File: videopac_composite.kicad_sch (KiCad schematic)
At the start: 17 parts, among them J102 Composite Output, J104 Composite Input, Q101 BC548, Q102 BC558, Q103 BC548

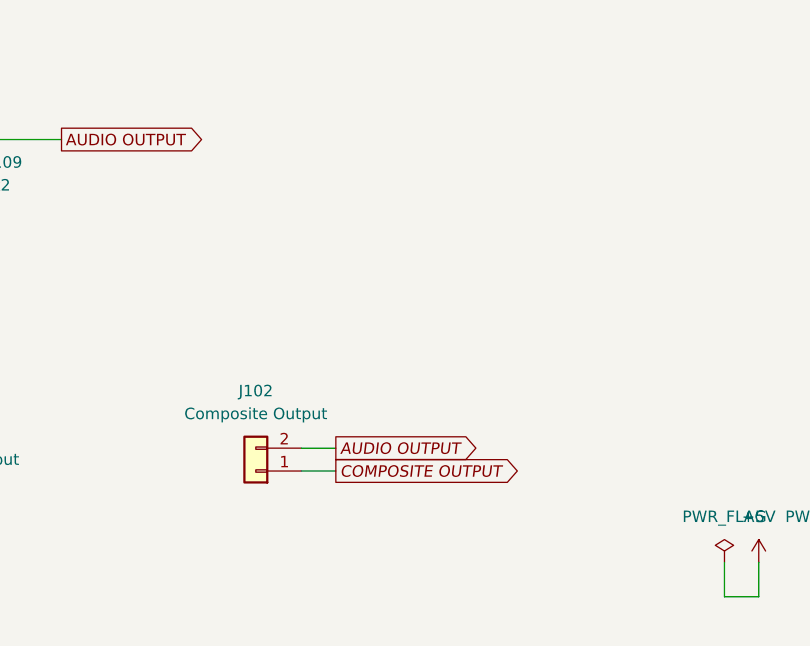
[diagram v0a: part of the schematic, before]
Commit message: Add additional ground connections.
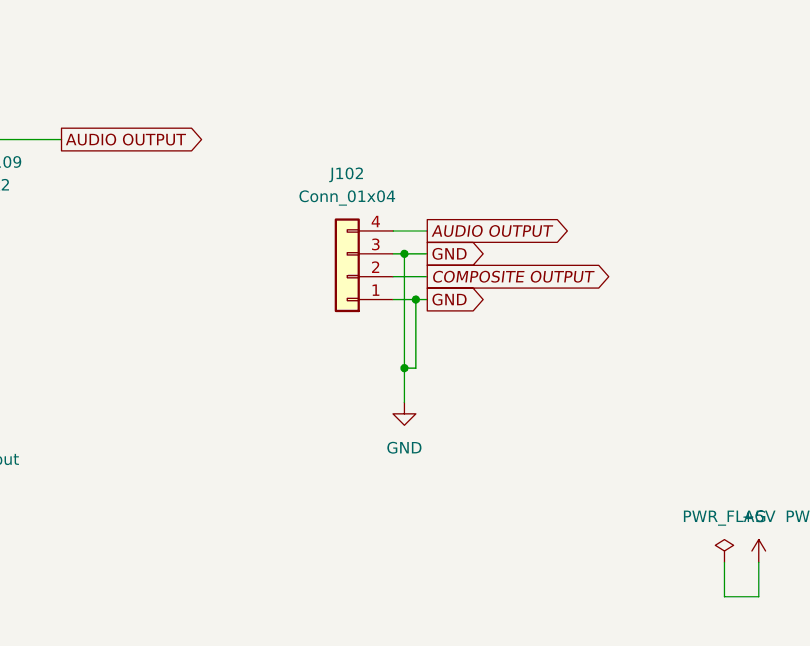
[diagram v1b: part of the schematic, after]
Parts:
- removed J102: Composite Output, Connector_PinHeader_2.54mm:PinHeader_1x02_P2.54mm_Horizontal, symbol Connector_Generic:Conn_01x02
- added J102: Conn_01x04, Connector_PinHeader_2.54mm:PinHeader_1x04_P2.54mm_Horizontal, symbol Connector_Generic:Conn_01x04
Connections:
- net AUDIO OUTPUT: now also J102.4 (Pin_4)
- net COMPOSITE OUTPUT: now also J102.2 (Pin_2)
- net GND: now also J102.1 (Pin_1), J102.3 (Pin_3)
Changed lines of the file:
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@@
   (junction (at 190.5 77.47) (diameter 0) (color 0 0 0 0)
   )
+  (junction (at 227.33 121.92) (diameter 0) (color 0 0 0 0)
+  )
+  (junction (at 226.06 116.84) (diameter 0) (color 0 0 0 0)
+  )
+  (junction (at 226.06 129.54) (diameter 0) (color 0 0 0 0)
+  )
+  (wire (pts (xy 224.79 119.38) (xy 228.6 119.38))
+    (stroke (width 0) (type default) (color 0 0 0 0))
+  )
   (wire (pts (xy 181.61 36.83) (xy 173.99 36.83))
     (stroke (width 0) (type default) (color 0 0 0 0))
   )
+  (wire (pts (xy 227.33 129.54) (xy 226.06 129.54))
+    (stroke (width 0) (type default) (color 0 0 0 0))
+  )
   (wire (pts (xy 152.4 64.77) (xy 152.4 67.31))
     (stroke (width 0) (type default) (color 0 0 0 0))
@@
     (stroke (width 0) (type default) (color 0 0 0 0))
   )
+  (wire (pts (xy 227.33 121.92) (xy 228.6 121.92))
+    (stroke (width 0) (type default) (color 0 0 0 0))
+  )
   (polyline (pts (xy 31.75 30.48) (xy 91.44 30.48))
     (stroke (width 0) (type default) (color 0 0 0 0))
@@
     (stroke (width 0) (type default) (color 0 0 0 0))
   )
-  (wire (pts (xy 214.63 138.43) (xy 218.44 138.43))
-    (stroke (width 0) (type default) (color 0 0 0 0))
-  )
-  (wire (pts (xy 214.63 140.97) (xy 218.44 140.97))
-    (stroke (width 0) (type default) (color 0 0 0 0))
-  )
   (wire (pts (xy 165.1 67.31) (xy 165.1 68.58))
     (stroke (width 0) (type default) (color 0 0 0 0))
@@
     (stroke (width 0) (type default) (color 0 0 0 0))
   )
+  (wire (pts (xy 226.06 129.54) (xy 226.06 133.35))
+    (stroke (width 0) (type default) (color 0 0 0 0))
+  )
+  (wire (pts (xy 226.06 116.84) (xy 228.6 116.84))
+    (stroke (width 0) (type default) (color 0 0 0 0))
+  )
   (wire (pts (xy 273.05 151.13) (xy 273.05 154.94))
     (stroke (width 0) (type default) (color 0 0 0 0))
@@
     (stroke (width 0) (type default) (color 0 0 0 0))
   )
+  (wire (pts (xy 224.79 116.84) (xy 226.06 116.84))
+    (stroke (width 0) (type default) (color 0 0 0 0))
+  )
   (wire (pts (xy 162.56 52.07) (xy 165.1 52.07))
     (stroke (width 0) (type default) (color 0 0 0 0))
@@
     (stroke (width 0) (type default) (color 0 0 0 0))
   )
+  (wire (pts (xy 224.79 121.92) (xy 227.33 121.92))
+    (stroke (width 0) (type default) (color 0 0 0 0))
+  )
   (wire (pts (xy 208.28 73.66) (xy 208.28 77.47))
     (stroke (width 0) (type default) (color 0 0 0 0))
   )
+  (wire (pts (xy 226.06 116.84) (xy 226.06 129.54))
+    (stroke (width 0) (type default) (color 0 0 0 0))
+  )
   (wire (pts (xy 208.28 62.23) (xy 212.09 62.23))
     (stroke (width 0) (type default) (color 0 0 0 0))
@@
     (stroke (width 0) (type default) (color 0 0 0 0))
   )
+  (wire (pts (xy 224.79 114.3) (xy 228.6 114.3))
+    (stroke (width 0) (type default) (color 0 0 0 0))
+  )
   (wire (pts (xy 190.5 77.47) (xy 190.5 80.01))
     (stroke (width 0) (type default) (color 0 0 0 0))
@@
   )
   (wire (pts (xy 152.4 67.31) (xy 165.1 67.31))
+    (stroke (width 0) (type default) (color 0 0 0 0))
+  )
+  (wire (pts (xy 227.33 121.92) (xy 227.33 129.54))
     (stroke (width 0) (type default) (color 0 0 0 0))
   )
@@
     )
   )
-  (global_label "COMPOSITE OUTPUT" (shape output) (at 218.44 140.97 0) (fields_autoplaced)
+  (global_label "COMPOSITE OUTPUT" (shape output) (at 228.6 119.38 0) (fields_autoplaced)
     (effects (font (size 1.27 1.27) italic) (justify left))
-    (property "Intersheet References" "${INTERSHEET_REFS}" (id 0) (at 239.8563 140.8906 0)
+    (property "Intersheet References" "${INTERSHEET_REFS}" (id 0) (at 250.0163 119.3006 0)
       (effects (font (size 1.27 1.27) italic) (justify left) hide)
     )
@@
     )
   )
-  (global_label "AUDIO OUTPUT" (shape output) (at 218.44 138.43 0) (fields_autoplaced)
+  (global_label "AUDIO OUTPUT" (shape output) (at 228.6 114.3 0) (fields_autoplaced)
     (effects (font (size 1.27 1.27) italic) (justify left))
-    (property "Intersheet References" "${INTERSHEET_REFS}" (id 0) (at 234.8973 138.3506 0)
+    (property "Intersheet References" "${INTERSHEET_REFS}" (id 0) (at 245.0573 114.2206 0)
       (effects (font (size 1.27 1.27) italic) (justify left) hide)
     )
@@
     )
   )
+  (global_label "GND" (shape output) (at 228.6 121.92 0) (fields_autoplaced)
+    (effects (font (size 1.27 1.27)) (justify left))
+    (property "Intersheet References" "${INTERSHEET_REFS}" (id 0) (at 234.8836 121.8406 0)
+      (effects (font (size 1.27 1.27)) (justify left) hide)
+    )
+  )
   (global_label "AUDIO INPUT" (shape input) (at 156.21 134.62 180) (fields_autoplaced)
     (effects (font (size 1.27 1.27) italic) (justify right))
@@
     )
   )
+  (global_label "GND" (shape output) (at 228.6 116.84 0) (fields_autoplaced)
+    (effects (font (size 1.27 1.27)) (justify left))
+    (property "Intersheet References" "${INTERSHEET_REFS}" (id 0) (at 234.8836 116.7606 0)
+      (effects (font (size 1.27 1.27)) (justify left) hide)
+    )
+  )
   (symbol (lib_id "power:PWR_FLAG") (at 261.62 151.13 0) (unit 1)
     (in_bom yes) (on_board yes) (fields_autoplaced)
@@
     (pin "2")
   )
-  (symbol (lib_id "Connector_Generic:Conn_01x02") (at 209.55 140.97 180) (unit 1)
-    (in_bom yes) (on_board yes) (fields_autoplaced)
-    (property "Reference" "J102" (id 0) (at 209.55 132.08 0))
-    (property "Value" "Composite Output" (id 1) (at 209.55 134.62 0))
-    (property "Footprint" "Connector_PinHeader_2.54mm:PinHeader_1x02_P2.54mm_Horizontal" (id 2) (at 209.55 140.97 0)
-      (effects (font (size 1.27 1.27)) hide)
-    )
-    (property "Datasheet" "~" (id 3) (at 209.55 140.97 0)
-      (effects (font (size 1.27 1.27)) hide)
-    )
-    (pin "1")
-    (pin "2")
-  )
   (symbol (lib_id "Device:R") (at 208.28 69.85 0) (unit 1)
     (in_bom yes) (on_board yes) (fields_autoplaced)
@@
     (pin "1")
   )
+  (symbol (lib_id "power:GND") (at 226.06 133.35 0) (unit 1)
+    (in_bom yes) (on_board yes) (fields_autoplaced)
+    (property "Reference" "#PWR04" (id 0) (at 226.06 139.7 0)
+      (effects (font (size 1.27 1.27)) hide)
+    )
+    (property "Value" "GND" (id 1) (at 226.06 138.43 0))
+    (property "Footprint" "" (id 2) (at 226.06 133.35 0)
+      (effects (font (size 1.27 1.27)) hide)
+    )
+    (property "Datasheet" "" (id 3) (at 226.06 133.35 0)
+      (effects (font (size 1.27 1.27)) hide)
+    )
+    (pin "1")
+  )
   (symbol (lib_id "Connector_Generic:Conn_01x04") (at 166.37 137.16 0) (unit 1)
     (in_bom yes) (on_board yes) (fields_autoplaced)
@@
     )
     (pin "1")
+  )
+  (symbol (lib_id "Connector_Generic:Conn_01x04") (at 219.71 119.38 180) (unit 1)
+    (in_bom yes) (on_board yes) (fields_autoplaced)
+    (property "Reference" "J102" (id 0) (at 219.71 107.95 0))
+    (property "Value" "Conn_01x04" (id 1) (at 219.71 110.49 0))
+    (property "Footprint" "Connector_PinHeader_2.54mm:PinHeader_1x04_P2.54mm_Horizontal" (id 2) (at 219.71 119.38 0)
+      (effects (font (size 1.27 1.27)) hide)
+    )
+    (property "Datasheet" "~" (id 3) (at 219.71 119.38 0)
+      (effects (font (size 1.27 1.27)) hide)
+    )
+    (pin "1")
+    (pin "2")
+    (pin "3")
+    (pin "4")
   )
   (symbol (lib_id "Transistor_BJT:BC558") (at 187.96 44.45 0) (unit 1)
@@
       (reference "#PWR03") (unit 1) (value "GND") (footprint "")
     )
+    (path "/bd247de0-7d2f-43b0-a3b6-041ae21a52c6"
+      (reference "#PWR04") (unit 1) (value "GND") (footprint "")
+    )
     (path "/d909f865-98a9-4d46-9787-a41c2f9d5a7e"
       (reference "#PWR0104") (unit 1) (value "GND") (footprint "")
@@
       (reference "D101") (unit 1) (value "1N4148") (footprint "Diode_THT:D_DO-35_SOD27_P7.62mm_Horizontal")
     )
-    (path "/2ccc8468-abf6-44bd-82d1-58c899e11aa2"
-      (reference "J102") (unit 1) (value "Composite Output") (footprint "Connector_PinHeader_2.54mm:PinHeader_1x02_P2.54mm_Horizontal")
+    (path "/dd7ae9c7-e47d-4f28-b899-d6d6d37bcbaf"
+      (reference "J102") (unit 1) (value "Conn_01x04") (footprint "Connector_PinHeader_2.54mm:PinHeader_1x04_P2.54mm_Horizontal")
     )
     (path "/c6dc5a2e-7543-4d95-8c42-986a5bb5b135"
